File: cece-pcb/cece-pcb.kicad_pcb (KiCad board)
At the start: 2 copper layers, 57 x 80.5 mm, 43 parts, among them J101 VAC, J102 HTU21D, J103 SERIAL, J104 Li-Ion Battery, K101 SANYOU_SRD_Form_C, Q101 Q_NPN, SW201 RES, U101 TLV75533PDBV, U102 MCP73811T-420I-OT, U201 ESP-12F

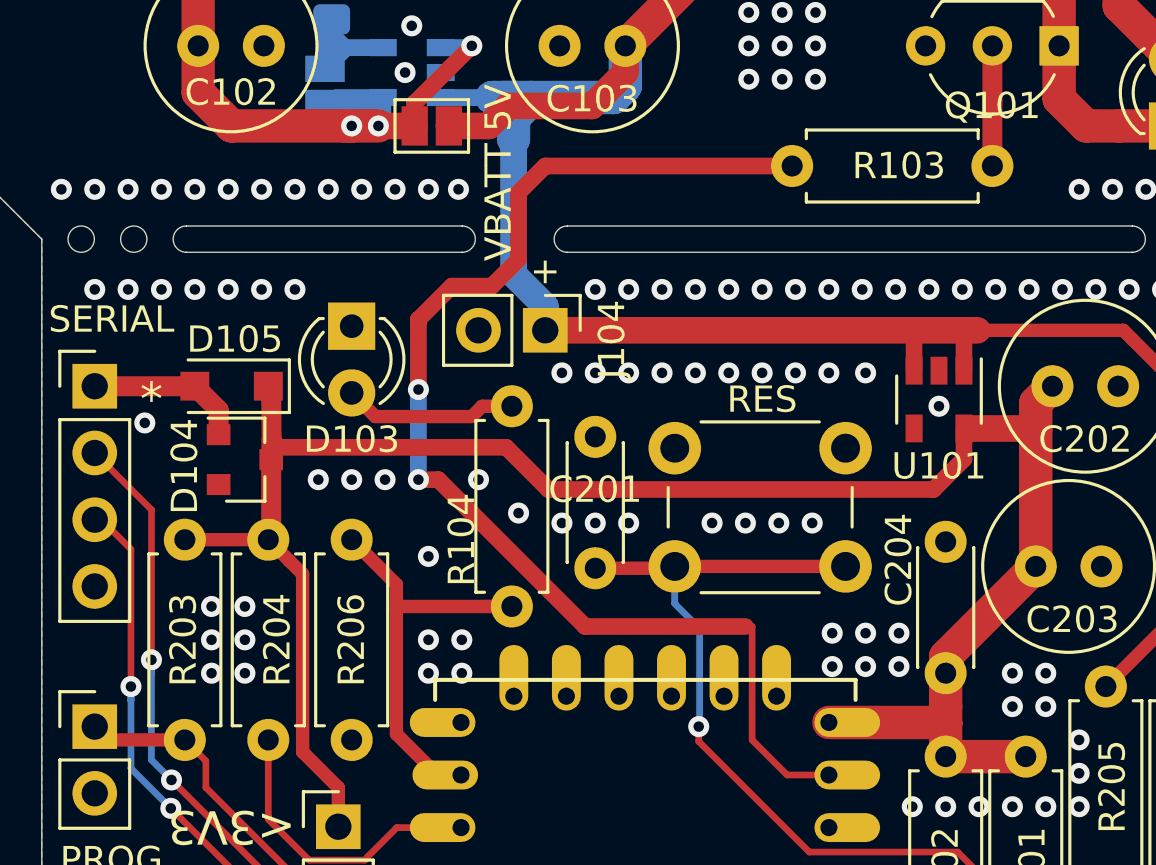
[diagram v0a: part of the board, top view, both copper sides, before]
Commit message: Add resistor to limit peak current in the reset pushbutton. Prevents contact welding
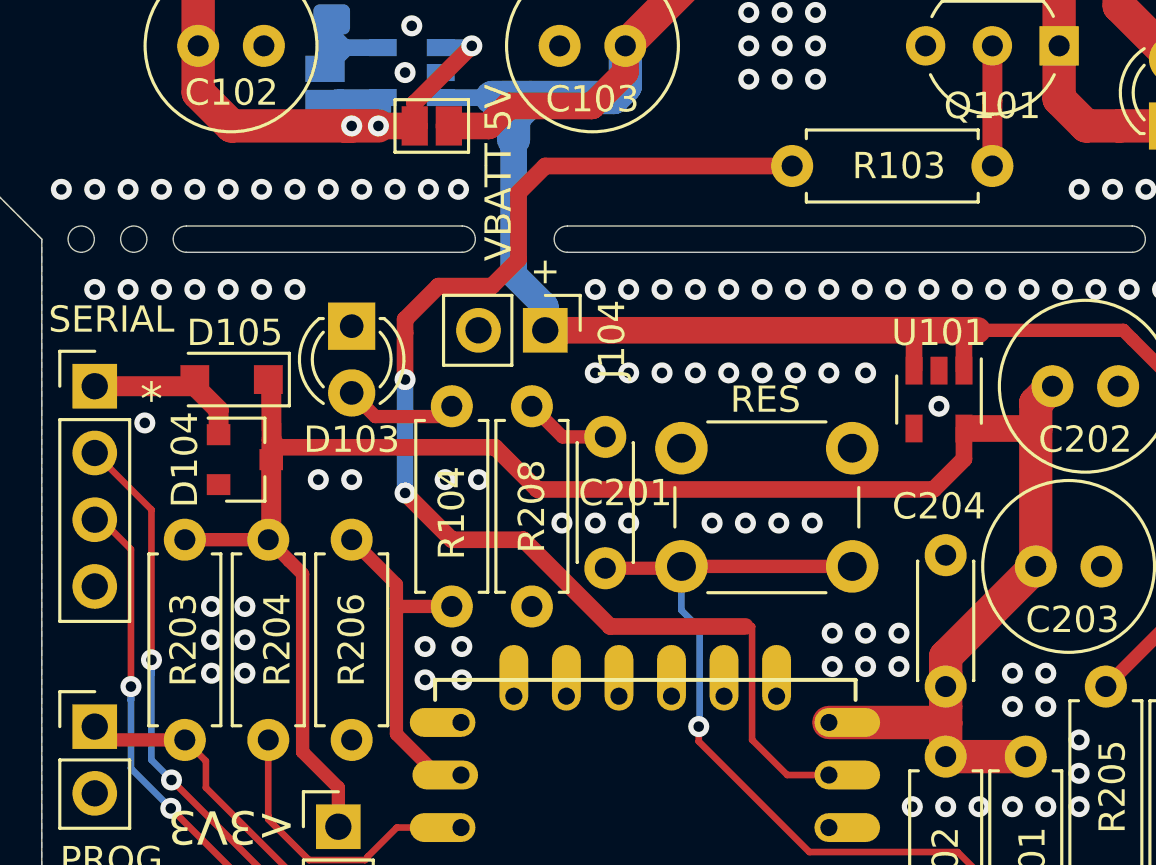
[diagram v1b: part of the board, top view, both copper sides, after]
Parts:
- added R208: 10k, Resistor_THT:R_Axial_DIN0207_L6.3mm_D2.5mm_P7.62mm_Horizontal, F.Cu at (136.7, 86.4)
- moved R104 2.29 mm to (133.6, 94.0)
- moved C204 0.51 mm to (152.4, 97.0)
- moved C201 0.38 mm to (139.4, 92.5)
- moved D105 0.25 mm to (125.2, 85.3)
- moved SW201 0.25 mm to (148.8, 92.5)
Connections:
- C201 pad 2: GND -> Net-(C201-Pad2)
- U101 pad 4: Net-(U101-Pad4) -> (no net)
- U201 pad 17: Net-(U201-Pad17) -> (no net)
- U201 pad 18: Net-(U201-Pad18) -> (no net)
- U201 pad 19: Net-(U201-Pad19) -> (no net)
- U201 pad 20: Net-(U201-Pad20) -> (no net)
- U201 pad 21: Net-(U201-Pad21) -> (no net)
- U201 pad 22: Net-(U201-Pad22) -> (no net)
- U201 pad 5: /ESP-12_common/D5|SCK -> (no net)
- U201 pad 6: /ESP-12_common/D6|MISO -> (no net)
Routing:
- net /ESP-12_common/D8: track 16.8 -> 12.8 mm
- net Net-(C201-Pad2): track 0.00 -> 3.43 mm
- net Net-(D103-Pad2): track 6.63 -> 4.35 mm
- net /RLY: track 47.6 -> 48.8 mm
- net GND: vias 181 -> 178

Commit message: Add EA cat signature
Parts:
- added REF**: a_black_cat, pol:a_black_cat, B.Cu at (131.1, 60.5)

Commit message: Use new stuff from pol lib
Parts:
- removed REF**: a_black_cat, pol:a_black_cat
- added EA101: a_black_cat, pol:a_black_cat, B.Cu at (131.1, 60.7)
- R208: value 10k -> 100
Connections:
- U101 pad 4: (no net) -> Net-(U101-Pad4)
- U201 pad 17: (no net) -> Net-(U201-Pad17)
- U201 pad 18: (no net) -> Net-(U201-Pad18)
- U201 pad 19: (no net) -> Net-(U201-Pad19)
- U201 pad 20: (no net) -> Net-(U201-Pad20)
- U201 pad 21: (no net) -> Net-(U201-Pad21)
- U201 pad 22: (no net) -> Net-(U201-Pad22)
- U201 pad 5: (no net) -> /ESP-12_common/D5|SCK
- U201 pad 6: (no net) -> /ESP-12_common/D6|MISO
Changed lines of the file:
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@@
-(kicad_pcb (version 20171130) (host pcbnew 5.1.9+dfsg1-1)
+(kicad_pcb (version 20171130) (host pcbnew "(5.1.5)-3")
   (general
     (thickness 1.6)
@@
     (tracks 438)
     (zones 0)
-    (modules 44)
-    (nets 30)
+    (modules 45)
+    (nets 39)
   )
   (page A4)
@@
   )
   (setup
-    (last_trace_width 0.635)
+    (last_trace_width 0.127)
     (user_trace_width 0.254)
     (user_trace_width 0.381)
@@
   (net 28 "Net-(JP103-Pad2)")
   (net 29 "Net-(C201-Pad2)")
+  (net 30 "Net-(U101-Pad4)")
+  (net 31 "Net-(U201-Pad22)")
+  (net 32 "Net-(U201-Pad21)")
+  (net 33 "Net-(U201-Pad20)")
+  (net 34 "Net-(U201-Pad19)")
+  (net 35 "Net-(U201-Pad18)")
+  (net 36 "Net-(U201-Pad17)")
+  (net 37 /ESP-12_common/D6|MISO)
+  (net 38 /ESP-12_common/D5|SCK)
   (net_class Default "This is the default net class."
     (clearance 0.254)
@@
     (add_net /ESP-12_common/D3)
     (add_net /ESP-12_common/D4)
+    (add_net /ESP-12_common/D5|SCK)
+    (add_net /ESP-12_common/D6|MISO)
     (add_net /ESP-12_common/D8)
     (add_net /ESP-12_common/EN)
@@
     (add_net "Net-(JP103-Pad2)")
     (add_net "Net-(Q101-Pad2)")
-  )
-  (module Resistor_THT:R_Axial_DIN0207_L6.3mm_D2.5mm_P7.62mm_Horizontal (layer F.Cu)
-    (at 136.652 86.36 270)
-    (descr "Resistor, Axial_DIN0207 series, Axial, Horizontal, pin pitch=7.62mm, 0.25W = 1/4W, length*diameter=6.3*2.5mm^2, http://cdn-reichelt.de/documents/datenblatt/B400/1_4W%23YAG.pdf")
-    (tags "Resistor Axial_DIN0207 series Axial Horizontal pin pitch 7.62mm 0.25W = 1/4W length 6.3mm diameter 2.5mm")
-    (fp_text reference R208 (at 3.81 0 270) (layer F.SilkS)
-      (effects (font (size 1 1) (thickness 0.15)))
-    )
-    (fp_text value 10k (at 3.81 2.37 90) (layer F.Fab)
-      (effects (font (size 1 1) (thickness 0.15)))
-    )
-    (fp_text user %R (at 3.81 0 90) (layer F.Fab)
-      (effects (font (size 1 1) (thickness 0.15)))
-    )
-    (fp_line (start 0.66 -1.25) (end 0.66 1.25) (layer F.Fab) (width 0.1))
-    (fp_line (start 0.66 1.25) (end 6.96 1.25) (layer F.Fab) (width 0.1))
-    (fp_line (start 6.96 1.25) (end 6.96 -1.25) (layer F.Fab) (width 0.1))
-    (fp_line (start 6.96 -1.25) (end 0.66 -1.25) (layer F.Fab) (width 0.1))
-    (fp_line (start 0 0) (end 0.66 0) (layer F.Fab) (width 0.1))
-    (fp_line (start 7.62 0) (end 6.96 0) (layer F.Fab) (width 0.1))
-    (fp_line (start 0.54 -1.04) (end 0.54 -1.37) (layer F.SilkS) (width 0.12))
-    (fp_line (start 0.54 -1.37) (end 7.08 -1.37) (layer F.SilkS) (width 0.12))
-    (fp_line (start 7.08 -1.37) (end 7.08 -1.04) (layer F.SilkS) (width 0.12))
-    (fp_line (start 0.54 1.04) (end 0.54 1.37) (layer F.SilkS) (width 0.12))
-    (fp_line (start 0.54 1.37) (end 7.08 1.37) (layer F.SilkS) (width 0.12))
-    (fp_line (start 7.08 1.37) (end 7.08 1.04) (layer F.SilkS) (width 0.12))
-    (fp_line (start -1.05 -1.5) (end -1.05 1.5) (layer F.CrtYd) (width 0.05))
-    (fp_line (start -1.05 1.5) (end 8.67 1.5) (layer F.CrtYd) (width 0.05))
-    (fp_line (start 8.67 1.5) (end 8.67 -1.5) (layer F.CrtYd) (width 0.05))
-    (fp_line (start 8.67 -1.5) (end -1.05 -1.5) (layer F.CrtYd) (width 0.05))
-    (pad 2 thru_hole oval (at 7.62 0 270) (size 1.6 1.6) (drill 0.8) (layers *.Cu *.Mask)
-      (net 1 GND))
-    (pad 1 thru_hole circle (at 0 0 270) (size 1.6 1.6) (drill 0.8) (layers *.Cu *.Mask)
-      (net 29 "Net-(C201-Pad2)"))
-    (model ${KISYS3DMOD}/Resistor_THT.3dshapes/R_Axial_DIN0207_L6.3mm_D2.5mm_P7.62mm_Horizontal.wrl
-      (at (xyz 0 0 0))
-      (scale (xyz 1 1 1))
-      (rotate (xyz 0 0 0))
-    )
-  )
-  (module pol:a_black_cat locked (layer B.Cu)
-    (at 131.064 60.452)
-    (fp_text reference REF** (at 0 -0.5) (layer Dwgs.User)
+    (add_net "Net-(U101-Pad4)")
+    (add_net "Net-(U201-Pad17)")
+    (add_net "Net-(U201-Pad18)")
+    (add_net "Net-(U201-Pad19)")
+    (add_net "Net-(U201-Pad20)")
+    (add_net "Net-(U201-Pad21)")
+    (add_net "Net-(U201-Pad22)")
+  )
+  (module pol:a_black_cat (layer B.Cu)
+    (at 131.064 60.706)
+    (fp_text reference EA101 (at 0 -0.5) (layer Dwgs.User)
       (effects (font (size 1 1) (thickness 0.15)))
     )
@@
     (fp_curve (pts (xy 1.549233 4.594787) (xy 1.567317 4.554495) (xy 1.585401 4.514202) (xy 1.601146 4.472989)) (layer B.SilkS) (width 0.16))
   )
+  (module Resistor_THT:R_Axial_DIN0207_L6.3mm_D2.5mm_P7.62mm_Horizontal (layer F.Cu)
+    (at 136.652 86.36 270)
+    (descr "Resistor, Axial_DIN0207 series, Axial, Horizontal, pin pitch=7.62mm, 0.25W = 1/4W, length*diameter=6.3*2.5mm^2, http://cdn-reichelt.de/documents/datenblatt/B400/1_4W%23YAG.pdf")
+    (tags "Resistor Axial_DIN0207 series Axial Horizontal pin pitch 7.62mm 0.25W = 1/4W length 6.3mm diameter 2.5mm")
+    (fp_text reference R208 (at 3.81 0 270) (layer F.SilkS)
+      (effects (font (size 1 1) (thickness 0.15)))
+    )
+    (fp_text value 100 (at 3.81 2.37 90) (layer F.Fab)
+      (effects (font (size 1 1) (thickness 0.15)))
+    )
+    (fp_text user %R (at 3.81 0 90) (layer F.Fab)
+      (effects (font (size 1 1) (thickness 0.15)))
+    )
+    (fp_line (start 0.66 -1.25) (end 0.66 1.25) (layer F.Fab) (width 0.1))
+    (fp_line (start 0.66 1.25) (end 6.96 1.25) (layer F.Fab) (width 0.1))
+    (fp_line (start 6.96 1.25) (end 6.96 -1.25) (layer F.Fab) (width 0.1))
+    (fp_line (start 6.96 -1.25) (end 0.66 -1.25) (layer F.Fab) (width 0.1))
+    (fp_line (start 0 0) (end 0.66 0) (layer F.Fab) (width 0.1))
+    (fp_line (start 7.62 0) (end 6.96 0) (layer F.Fab) (width 0.1))
+    (fp_line (start 0.54 -1.04) (end 0.54 -1.37) (layer F.SilkS) (width 0.12))
+    (fp_line (start 0.54 -1.37) (end 7.08 -1.37) (layer F.SilkS) (width 0.12))
+    (fp_line (start 7.08 -1.37) (end 7.08 -1.04) (layer F.SilkS) (width 0.12))
+    (fp_line (start 0.54 1.04) (end 0.54 1.37) (layer F.SilkS) (width 0.12))
+    (fp_line (start 0.54 1.37) (end 7.08 1.37) (layer F.SilkS) (width 0.12))
+    (fp_line (start 7.08 1.37) (end 7.08 1.04) (layer F.SilkS) (width 0.12))
+    (fp_line (start -1.05 -1.5) (end -1.05 1.5) (layer F.CrtYd) (width 0.05))
+    (fp_line (start -1.05 1.5) (end 8.67 1.5) (layer F.CrtYd) (width 0.05))
+    (fp_line (start 8.67 1.5) (end 8.67 -1.5) (layer F.CrtYd) (width 0.05))
+    (fp_line (start 8.67 -1.5) (end -1.05 -1.5) (layer F.CrtYd) (width 0.05))
+    (pad 2 thru_hole oval (at 7.62 0 270) (size 1.6 1.6) (drill 0.8) (layers *.Cu *.Mask)
+      (net 1 GND))
+    (pad 1 thru_hole circle (at 0 0 270) (size 1.6 1.6) (drill 0.8) (layers *.Cu *.Mask)
+      (net 29 "Net-(C201-Pad2)"))
+    (model ${KISYS3DMOD}/Resistor_THT.3dshapes/R_Axial_DIN0207_L6.3mm_D2.5mm_P7.62mm_Horizontal.wrl
+      (at (xyz 0 0 0))
+      (scale (xyz 1 1 1))
+      (rotate (xyz 0 0 0))
+    )
+  )
   (module Jumper:SolderJumper-2_P1.3mm_Open_Pad1.0x1.5mm (layer B.Cu)
     (at 128.778 74.168 90)
@@
       (effects (font (size 1 1) (thickness 0.15)))
     )
-    (pad 22 thru_hole oval (at 11.99 15 270) (size 2.5 1.1) (drill 0.65 (offset -0.7 0)) (layers *.Cu *.Mask F.SilkS))
-    (pad 21 thru_hole oval (at 9.99 15 270) (size 2.5 1.1) (drill 0.65 (offset -0.7 0)) (layers *.Cu *.Mask F.SilkS))
-    (pad 20 thru_hole oval (at 7.99 15 270) (size 2.5 1.1) (drill 0.65 (offset -0.7 0)) (layers *.Cu *.Mask F.SilkS))
-    (pad 19 thru_hole oval (at 5.99 15 270) (size 2.5 1.1) (drill 0.65 (offset -0.7 0)) (layers *.Cu *.Mask F.SilkS))
-    (pad 18 thru_hole oval (at 3.99 15 270) (size 2.5 1.1) (drill 0.65 (offset -0.7 0)) (layers *.Cu *.Mask F.SilkS))
-    (pad 17 thru_hole oval (at 1.99 15 270) (size 2.5 1.1) (drill 0.65 (offset -0.7 0)) (layers *.Cu *.Mask F.SilkS))
+    (pad 22 thru_hole oval (at 11.99 15 270) (size 2.5 1.1) (drill 0.65 (offset -0.7 0)) (layers *.Cu *.Mask F.SilkS)
+      (net 31 "Net-(U201-Pad22)"))
+    (pad 21 thru_hole oval (at 9.99 15 270) (size 2.5 1.1) (drill 0.65 (offset -0.7 0)) (layers *.Cu *.Mask F.SilkS)
+      (net 32 "Net-(U201-Pad21)"))
+    (pad 20 thru_hole oval (at 7.99 15 270) (size 2.5 1.1) (drill 0.65 (offset -0.7 0)) (layers *.Cu *.Mask F.SilkS)
+      (net 33 "Net-(U201-Pad20)"))
+    (pad 19 thru_hole oval (at 5.99 15 270) (size 2.5 1.1) (drill 0.65 (offset -0.7 0)) (layers *.Cu *.Mask F.SilkS)
+      (net 34 "Net-(U201-Pad19)"))
+    (pad 18 thru_hole oval (at 3.99 15 270) (size 2.5 1.1) (drill 0.65 (offset -0.7 0)) (layers *.Cu *.Mask F.SilkS)
+      (net 35 "Net-(U201-Pad18)"))
+    (pad 17 thru_hole oval (at 1.99 15 270) (size 2.5 1.1) (drill 0.65 (offset -0.7 0)) (layers *.Cu *.Mask F.SilkS)
+      (net 36 "Net-(U201-Pad17)"))
     (pad 16 thru_hole oval (at 14 0 180) (size 2.5 1.1) (drill 0.65 (offset 0.7 0)) (layers *.Cu *.Mask F.SilkS)
       (net 7 /TX))
@@
     (pad 7 thru_hole oval (at 0 12 180) (size 2.5 1.1) (drill 0.65 (offset -0.7 0)) (layers *.Cu *.Mask F.SilkS)
       (net 13 /RLY))
-    (pad 6 thru_hole oval (at 0 10 180) (size 2.5 1.1) (drill 0.65 (offset -0.7 0)) (layers *.Cu *.Mask F.SilkS))
-    (pad 5 thru_hole oval (at 0 8 180) (size 2.5 1.1) (drill 0.65 (offset -0.7 0)) (layers *.Cu *.Mask F.SilkS))
+    (pad 6 thru_hole oval (at 0 10 180) (size 2.5 1.1) (drill 0.65 (offset -0.7 0)) (layers *.Cu *.Mask F.SilkS)
+      (net 37 /ESP-12_common/D6|MISO))
+    (pad 5 thru_hole oval (at 0 8 180) (size 2.5 1.1) (drill 0.65 (offset -0.7 0)) (layers *.Cu *.Mask F.SilkS)
+      (net 38 /ESP-12_common/D5|SCK))
     (pad 4 thru_hole oval (at 0 6 180) (size 2.5 1.1) (drill 0.65 (offset -0.7 0)) (layers *.Cu *.Mask F.SilkS)
       (net 20 /ESP-12_common/D0))
@@
     (pad 5 smd rect (at 1.1 -0.95 270) (size 1.06 0.65) (layers F.Cu F.Paste F.Mask)
       (net 3 +3V3))
-    (pad 4 smd rect (at 1.1 0.95 270) (size 1.06 0.65) (layers F.Cu F.Paste F.Mask))
+    (pad 4 smd rect (at 1.1 0.95 270) (size 1.06 0.65) (layers F.Cu F.Paste F.Mask)
+      (net 30 "Net-(U101-Pad4)"))
     (pad 3 smd rect (at -1.1 0.95 270) (size 1.06 0.65) (layers F.Cu F.Paste F.Mask)
       (net 5 +BATT))
